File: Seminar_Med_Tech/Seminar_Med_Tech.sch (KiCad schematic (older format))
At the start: 72 parts, among them J1 CONN_02X08, U1 JP22, U10 JP31, U11 JP32, U12 JP33, U13 JP34, U14 J5, U15 JP35, U16 JP36, U17 JP37, U18 ADS1298, U19 OPA2340, U2 JP23, U20 ADS1298, U3 JP24, U4 JP25, U5 JP26, U6 JP27, U7 JP28, U8 JP29, U9 JP30

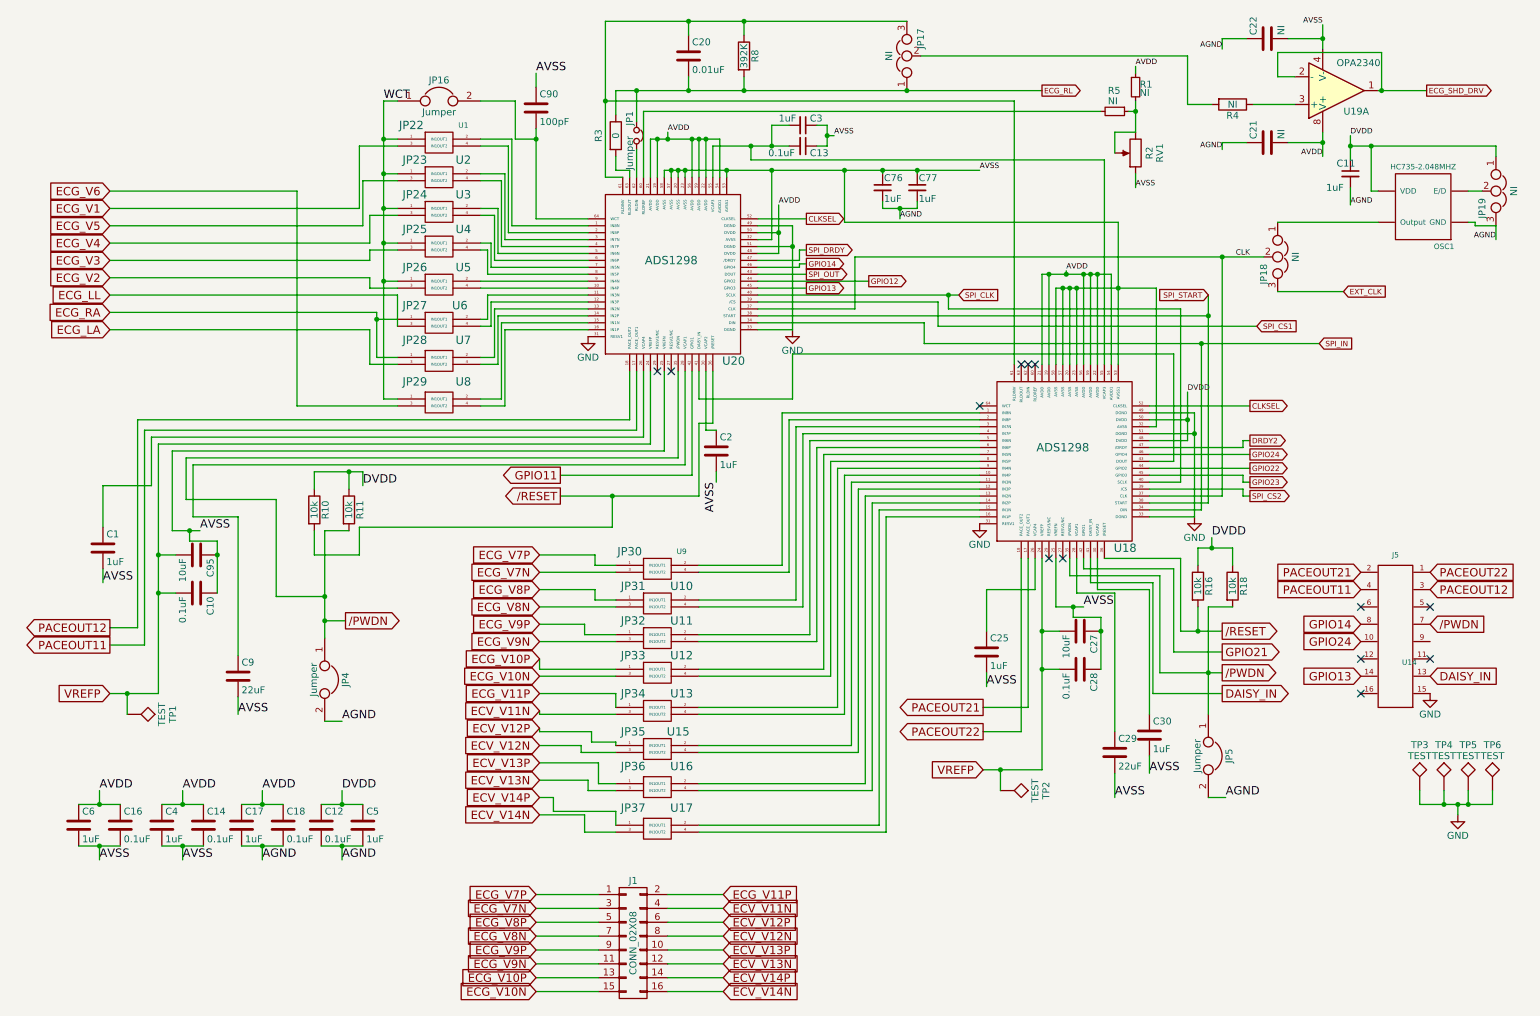
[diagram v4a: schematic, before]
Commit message: Changed labels
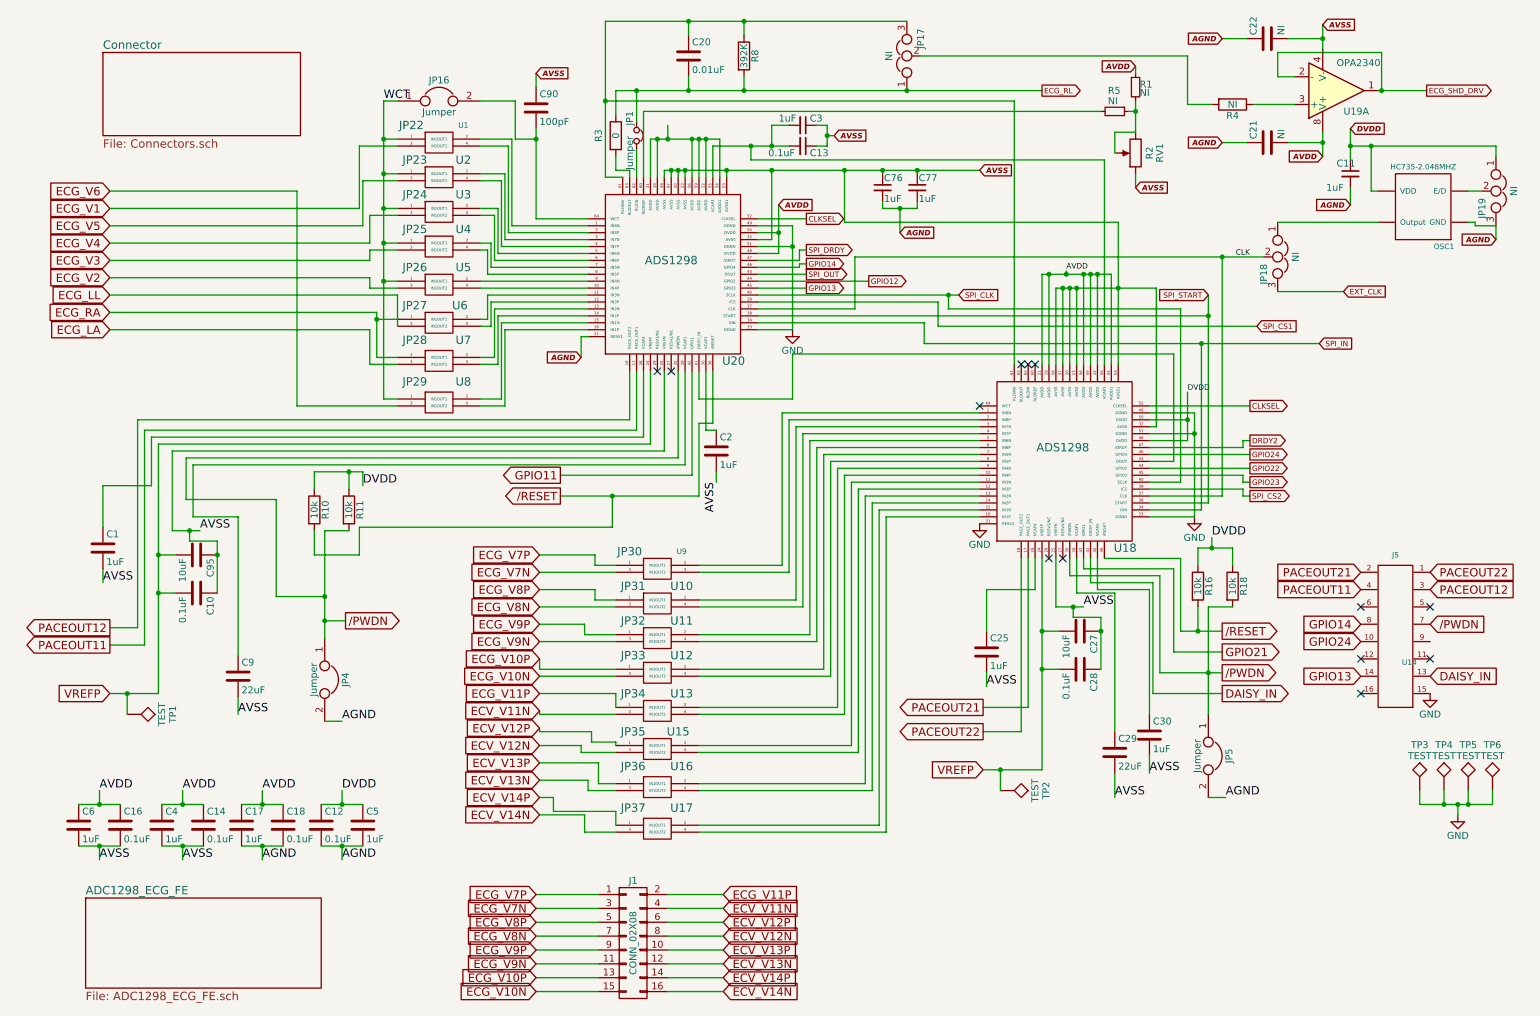
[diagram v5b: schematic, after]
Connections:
- net AGND: now also U20.31 (RESV1)
- net AVDD: no longer U20.19 (AVDD), U20.21 (AVDD), U20.22 (AVDD), U20.54 (AVDD1), U20.56 (AVDD), U20.59 (AVDD)
- net GND: no longer U20.31 (RESV1)
- new net: U20.19 (AVDD), U20.21 (AVDD), U20.22 (AVDD), U20.54 (AVDD1), U20.56 (AVDD), U20.59 (AVDD)
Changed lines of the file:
@@
 $Descr A4 11693 8268
 encoding utf-8
-Sheet 1 1
+Sheet 1 3
 Title ""
 Date ""
@@
 	1    0    0    -1
 $EndComp
-Text Label 4150 975  0    60   ~ 0
-AVSS
 $Comp
 L ADS1298 U20
@@
 Text Label 9300 2300 2    39   ~ 0
 CLK
-$Comp
-L GND #PWR02
-U 1 1 592AF0AE
-P 4525 2875
-F 0 "#PWR02" H 4525 2625 50  0001 C CNN
-F 1 "GND" H 4525 2725 50  0000 C CNN
-F 2 "" H 4525 2875 50  0001 C CNN
-F 3 "" H 4525 2875 50  0001 C CNN
-	1    4525 2875
-	1    0    0    -1
-$EndComp
 Text GLabel 7375 6000 0    60   Input ~ 0
 VREFP
@@
 	1    0    0    1
 $EndComp
-Text Label 9825 1575 2    39   ~ 0
-AVDD
 $Comp
 L C C21
@@
 	0    -1   -1   0
 $EndComp
-Text Label 9100 1525 2    39   ~ 0
-AGND
-Text Label 9825 625  2    39   ~ 0
-AVSS
 $Comp
 L C C22
@@
 Text GLabel 10575 1100 2    39   Output ~ 0
 ECG_SHD_DRV
-Text Label 9100 800  2    39   ~ 0
-AGND
 $Comp
 L R R4
@@
 Text GLabel 7800 1100 2    39   Output ~ 0
 ECG_RL
-Text Label 5100 1400 0    39   ~ 0
-AVDD
 $Comp
 L C_Small C13
@@
 	0    1    1    0
 $EndComp
-Text Label 6300 1425 0    39   ~ 0
-AVSS
 $Comp
 L C_Small C76
@@
 	1    0    0    -1
 $EndComp
-Text Label 6775 2025 0    39   ~ 0
-AGND
-Text Label 7350 1675 0    39   ~ 0
-AVSS
 Text Label 7975 2400 0    39   ~ 0
 AVDD
@@
 	1    0    0    -1
 $EndComp
-Text Label 8475 925  0    39   ~ 0
-AVDD
-Text Label 8475 1800 0    39   ~ 0
-AVSS
 $Comp
 L Jumper_NC_Dual JP18
@@
 	0    1    1    0
 $EndComp
-Text Label 11075 2175 2    39   ~ 0
-AGND
 $Comp
 L C_Small C11
@@
 	1    0    0    -1
 $EndComp
-Text Label 10025 1425 0    39   ~ 0
-DVDD
-Text Label 10025 1925 0    39   ~ 0
-AGND
-Text Label 5900 1925 0    39   ~ 0
-AVDD
 Text Label 8850 3275 0    39   ~ 0
 DVDD
@@
 Text Label 2750 5650 0    60   ~ 0
 AGND
+$Sheet
+S 1025 825  1425 600
+U 59470A40
+F0 "Connector" 60
+F1 "Connectors.sch" 60
+$EndSheet
+$Sheet
+S 900  6925 1700 650
+U 59470E15
+F0 "ADC1298_ECG_FE" 60
+F1 "ADC1298_ECG_FE.sch" 60
+$EndSheet
+Text GLabel 9825 625  2    39   Input Italic 8
+AVSS
+Text GLabel 9100 725  0    39   Input Italic 8
+AGND
+Text GLabel 9100 1475 0    39   Input Italic 8
+AGND
+Text GLabel 9825 1575 0    39   Input Italic 8
+AVDD
+Text GLabel 10025 1375 2    39   Input Italic 8
+DVDD
+Text GLabel 10025 1925 0    39   Input Italic 8
+AGND
+Text GLabel 11075 2175 0    39   Input Italic 8
+AGND
+Text GLabel 8475 1800 2    39   Input Italic 8
+AVSS
+Text GLabel 8475 925  0    39   Input Italic 8
+AVDD
+Text GLabel 6300 1425 2    39   Input Italic 8
+AVSS
+Text GLabel 7350 1675 2    39   Input Italic 8
+AVSS
+Text GLabel 6775 2125 2    39   Input Italic 8
+AGND
+Text GLabel 5900 1925 2    39   Input Italic 8
+AVDD
+Text GLabel 4150 975  2    39   Input Italic 8
+AVSS
+Text GLabel 4475 3025 0    39   Input Italic 8
+AGND
 Connection ~ 3000 2750
 Connection ~ 4150 1450
@@
 Connection ~ 9825 725
 Wire Wire Line
-	9275 725  9100 725
-Wire Wire Line
-	9100 725  9100 800
-Wire Wire Line
-	9275 1475 9100 1475
-Wire Wire Line
-	9100 1475 9100 1525
+	9100 725  9275 725
+Wire Wire Line
+	9100 1475 9275 1475
 Wire Wire Line
 	9625 1200 9325 1200
@@
 Connection ~ 5025 1450
 Wire Wire Line
-	5100 1450 5100 1400
+	5100 1350 5100 1450
 Connection ~ 5100 1450
 Wire Wire Line
@@
 	6900 1950 6900 1900
 Wire Wire Line
-	6775 1950 6775 2025
+	6775 1950 6775 2125
 Connection ~ 6775 1950
 Wire Wire Line
@@
 Connection ~ 10175 1500
 Wire Wire Line
-	10025 1425 10025 1600
+	10025 1375 10025 1600
 Wire Wire Line
 	10025 1800 10025 1925
@@
 Wire Wire Line
 	2550 4450 2875 4450
+Wire Wire Line
+	4525 2875 4475 2875
+Wire Wire Line
+	4475 2875 4475 3025
 $EndSCHEMATC

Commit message: Changed labels in ADC1298_ECG_FE
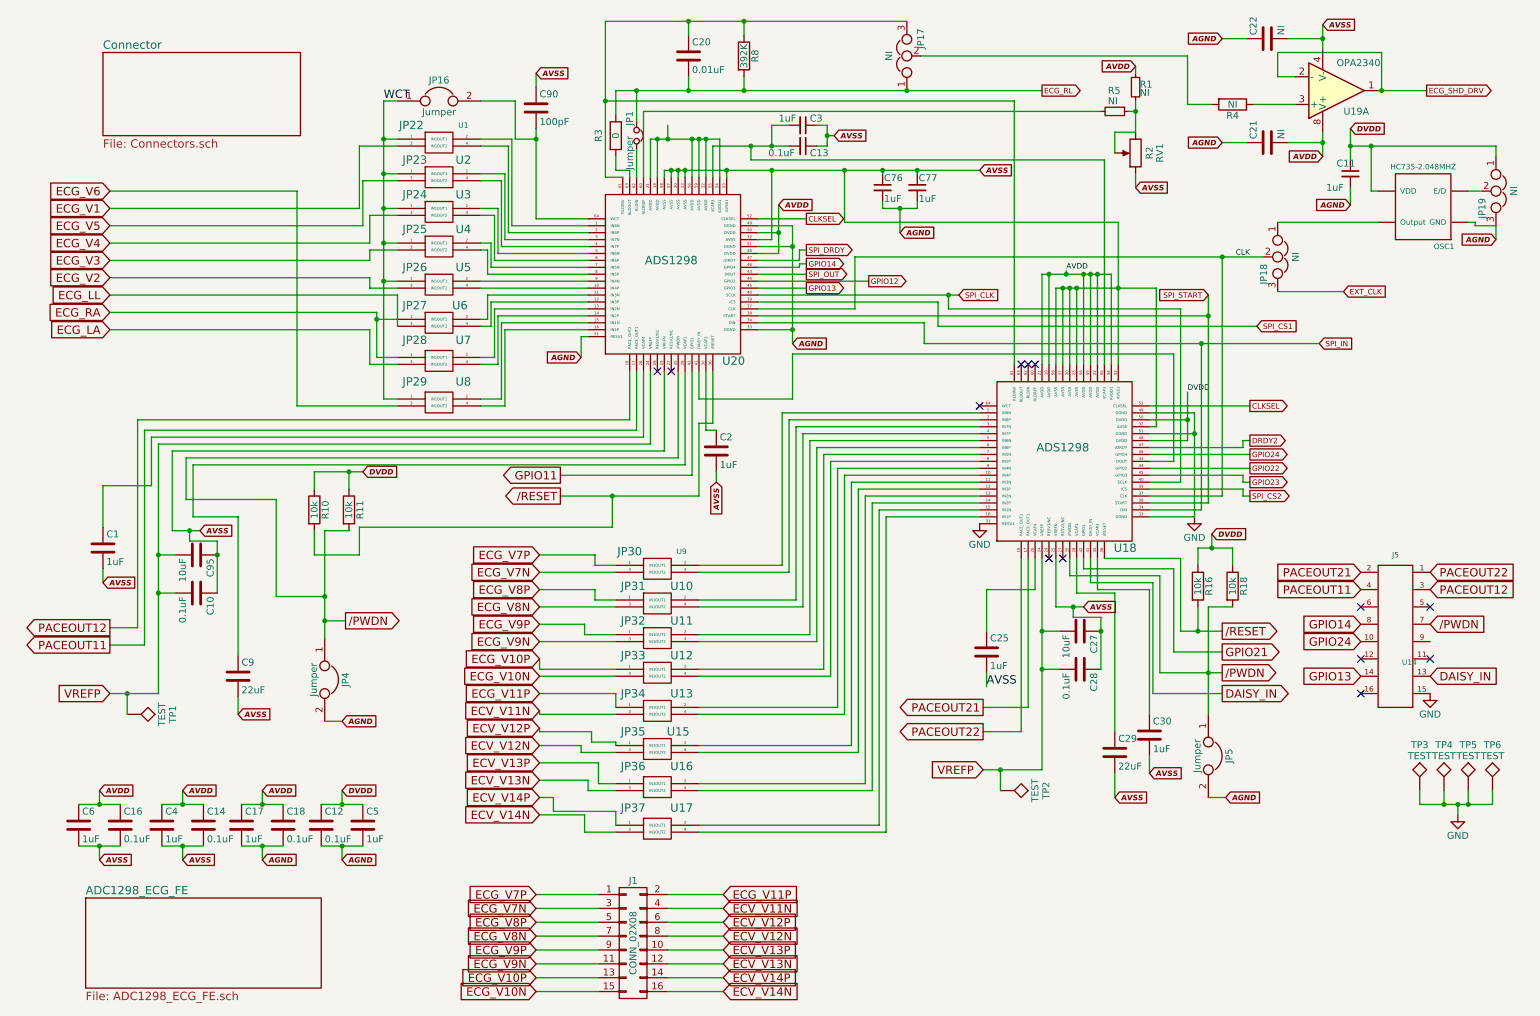
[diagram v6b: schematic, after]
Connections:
- net AGND: now also U20.33 (DGND), U20.49 (DGND), U20.51 (DGND)
- net GND: no longer U20.33 (DGND), U20.49 (DGND), U20.51 (DGND)
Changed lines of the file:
@@
 	0    1    1    0
 $EndComp
-Text Label 9025 4325 0    60   ~ 0
-DVDD
 $Comp
 L C C30
@@
 	1    0    0    -1
 $EndComp
-Text Label 8575 6025 0    60   ~ 0
-AVSS
 $Comp
 L C C29
@@
 	1    0    0    -1
 $EndComp
-Text Label 8325 6200 0    60   ~ 0
-AVSS
 $Comp
 L C C25
@@
 $EndComp
 Text Label 7400 5400 0    60   ~ 0
-AVSS
-Text Label 8100 4825 0    60   ~ 0
 AVSS
 $Comp
@@
 	1    0    0    -1
 $EndComp
-Text Label 5450 3925 3    60   ~ 0
-AVSS
 $Comp
 L C C9
@@
 	1    0    0    -1
 $EndComp
-Text Label 2000 5600 0    60   ~ 0
-AVSS
 $Comp
 L C C1
@@
 	1    0    0    -1
 $EndComp
-Text Label 1025 4650 0    60   ~ 0
-AVSS
-Text Label 1725 4275 0    60   ~ 0
-AVSS
 $Comp
 L TEST TP1
@@
 	0    1    1    0
 $EndComp
-Text Label 2900 3950 0    60   ~ 0
-DVDD
 NoConn ~ 5025 3125
 NoConn ~ 5125 3125
 NoConn ~ 7350 3375
-$Comp
-L GND #PWR03
-U 1 1 592C9248
-P 6000 2825
-F 0 "#PWR03" H 6000 2575 50  0001 C CNN
-F 1 "GND" H 6000 2675 50  0000 C CNN
-F 2 "" H 6000 2825 50  0001 C CNN
-F 3 "" H 6000 2825 50  0001 C CNN
-	1    6000 2825
-	1    0    0    -1
-$EndComp
 $Comp
 L GND #PWR04
@@
 	1    0    0    -1
 $EndComp
-Text Label 1000 6150 0    60   ~ 0
-AVDD
-Text Label 1000 6650 0    60   ~ 0
-AVSS
 $Comp
 L C C4
@@
 	1    0    0    -1
 $EndComp
-Text Label 1600 6150 0    60   ~ 0
-AVDD
-Text Label 1600 6650 0    60   ~ 0
-AVSS
 $Comp
 L C C17
@@
 	1    0    0    -1
 $EndComp
-Text Label 2175 6150 0    60   ~ 0
-AVDD
-Text Label 2175 6650 0    60   ~ 0
-AGND
 $Comp
 L C C12
@@
 	1    0    0    -1
 $EndComp
-Text Label 2750 6150 0    60   ~ 0
-DVDD
-Text Label 2750 6650 0    60   ~ 0
-AGND
 $Comp
 L OPA2340 U19
@@
 Text GLabel 5500 7600 2    60   Input ~ 0
 ECV_V14N
-Text Label 9125 6200 0    60   ~ 0
-AGND
 Text Label 3050 1175 0    60   ~ 0
 WCT
-Text Label 2750 5650 0    60   ~ 0
-AGND
 $Sheet
 S 1025 825  1425 600
@@
 Text GLabel 4475 3025 0    39   Input Italic 8
 AGND
+Text GLabel 6000 2925 2    39   Input Italic 8
+AGND
+Text GLabel 2900 3850 2    39   Input Italic 8
+DVDD
+Text GLabel 1725 4275 2    39   Input Italic 8
+AVSS
+Text GLabel 1025 4650 2    39   Input Italic 8
+AVSS
+Text GLabel 5450 3925 3    39   Input Italic 8
+AVSS
+Text GLabel 2000 5600 2    39   Input Italic 8
+AVSS
+Text GLabel 2750 5650 2    39   Input Italic 8
+AGND
+Text GLabel 9025 4300 2    39   Input Italic 8
+DVDD
 Connection ~ 3000 2750
 Connection ~ 4150 1450
@@
 	9000 6200 9125 6200
 Wire Wire Line
-	9025 4325 9025 4400
+	9025 4300 9025 4400
 Connection ~ 9025 4400
 Wire Wire Line
@@
 Wire Wire Line
 	2550 3850 2900 3850
-Wire Wire Line
-	2900 3850 2900 3950
 Connection ~ 2800 3850
 Wire Wire Line
@@
 	5750 2075 6000 2075
 Wire Wire Line
-	6000 2075 6000 2825
+	6000 2075 6000 2925
 Wire Wire Line
 	6000 2825 5750 2825
@@
 Wire Wire Line
 	4475 2875 4475 3025
+Connection ~ 6000 2825
+Text GLabel 8100 4825 2    39   Input Italic 8
+AVSS
+Text GLabel 9125 6200 2    39   Input Italic 8
+AGND
+Text GLabel 8325 6200 2    39   Input Italic 8
+AVSS
+Text GLabel 8575 6025 2    39   Input Italic 8
+AVSS
+Text GLabel 2750 6150 2    39   Input Italic 8
+DVDD
+Text GLabel 2750 6650 2    39   Input Italic 8
+AGND
+Text GLabel 2175 6650 2    39   Input Italic 8
+AGND
+Text GLabel 2175 6150 2    39   Input Italic 8
+AVDD
+Text GLabel 1600 6150 2    39   Input Italic 8
+AVDD
+Text GLabel 1000 6150 2    39   Input Italic 8
+AVDD
+Text GLabel 1600 6650 2    39   Input Italic 8
+AVSS
+Text GLabel 1000 6650 2    39   Input Italic 8
+AVSS
 $EndSCHEMATC

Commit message: Update
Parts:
- removed U14: J5, symbol Header12
- removed U19: OPA2340, symbol OPA2340
- added J7: CONN_02X08, symbol CONN_02X08
- added R15, R75: 10K, symbol R_Small
- added U1: OPA132, symbol OPA132
- JP22: renamed from U1; value JP22 -> JP2x2
- JP23: renamed from U2; value JP23 -> JP2x2
- JP24: renamed from U3; value JP24 -> JP2x2
- JP25: renamed from U4; value JP25 -> JP2x2
- JP26: renamed from U5; value JP26 -> JP2x2
- JP27: renamed from U6; value JP27 -> JP2x2
- JP28: renamed from U7; value JP28 -> JP2x2
- JP29: renamed from U8; value JP29 -> JP2x2
- JP30: renamed from U9; value JP30 -> JP2x2
- JP31: renamed from U10; value JP31 -> JP2x2
- JP32: renamed from U11; value JP32 -> JP2x2
- JP33: renamed from U12; value JP33 -> JP2x2
- JP34: renamed from U13; value JP34 -> JP2x2
- JP35: renamed from U15; value JP35 -> JP2x2
- JP36: renamed from U16; value JP36 -> JP2x2
- JP37: renamed from U17; value JP37 -> JP2x2
- R2: renamed from RV1; value R2 -> NI
- renumbered C28 to C15, C29 to C19, C30 to C25, C25 to C7, C27 to C8, R16 to R11, R18 to R12, R10 to R6, R11 to R7
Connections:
- net GND is gone; now on net AGND: TP3.1, TP4.1, TP5.1, TP6.1, U18.31 (RESV1), U18.33 (DGND), U18.49 (DGND), U18.51 (DGND)
- net /PWDN: now also J7.8 (P8)
- net AGND: now also J7.16 (P16)
- net AVDD: now also U20.19 (AVDD), U20.21 (AVDD), U20.22 (AVDD), U20.54 (AVDD1), U20.56 (AVDD), U20.59 (AVDD), U1.7 (V+); no longer U20.48 (DVDD), U20.50 (DVDD)
- net AVSS: now also U1.4 (V-)
- net DAISY_IN: now also J7.14 (P14)
- net DVDD: now also U20.48 (DVDD), U20.50 (DVDD), R15.1, R75.1
- net ECG_SHD_DRV: now also U1.2 (-), U1.6
- net GPIO13: now also J7.5 (P5)
- net GPIO14: now also J7.7 (P7)
- net GPIO23: now also J7.10 (P10)
- net GPIO24: now also J7.9 (P9)
- net PACEOUT11: now also J7.3 (P3)
- net PACEOUT12: now also J7.4 (P4)
- net PACEOUT21: now also J7.1 (P1)
- net PACEOUT22: now also J7.2 (P2)
- net SPI_CS1: now also R75.2
- net SPI_CS2: now also R15.2
- net at R4.1: now also U1.3 (+)

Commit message: jumper
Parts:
- C1, C10, C11, C12, C13, C14, C15, C16, C17, C18, C19, C2, C20, C21, C22, C25, C3, C4, C5, C6, C7, C76, C77, C8, C9, C90, C95: footprint (none) -> Capacitors_SMD:C_1206_HandSoldering
- J1, J7: footprint (none) -> Pin_Headers:Pin_Header_Straight_2x08_Pitch2.54mm
- JP1, JP16, JP4, JP5: footprint (none) -> jumper:Jumper1x2
- JP17, JP18, JP19: footprint (none) -> jumper:jumper1x3
- R1, R11, R12, R15, R2, R3, R4, R5, R6, R7, R75, R8: footprint (none) -> Resistors_SMD:R_0805_HandSoldering
- TP1, TP2, TP3, TP4, TP5, TP6: footprint (none) -> Measurement_Points:Test_Point_Keystone_5000-5004_Miniature
